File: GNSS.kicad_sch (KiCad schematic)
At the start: 16 parts, among them J10 USB_C_USB2.0_16P, J11 Micro_SD_Card, J12 RF SMA, SW3 SW_Push, U6 NEO-M9N

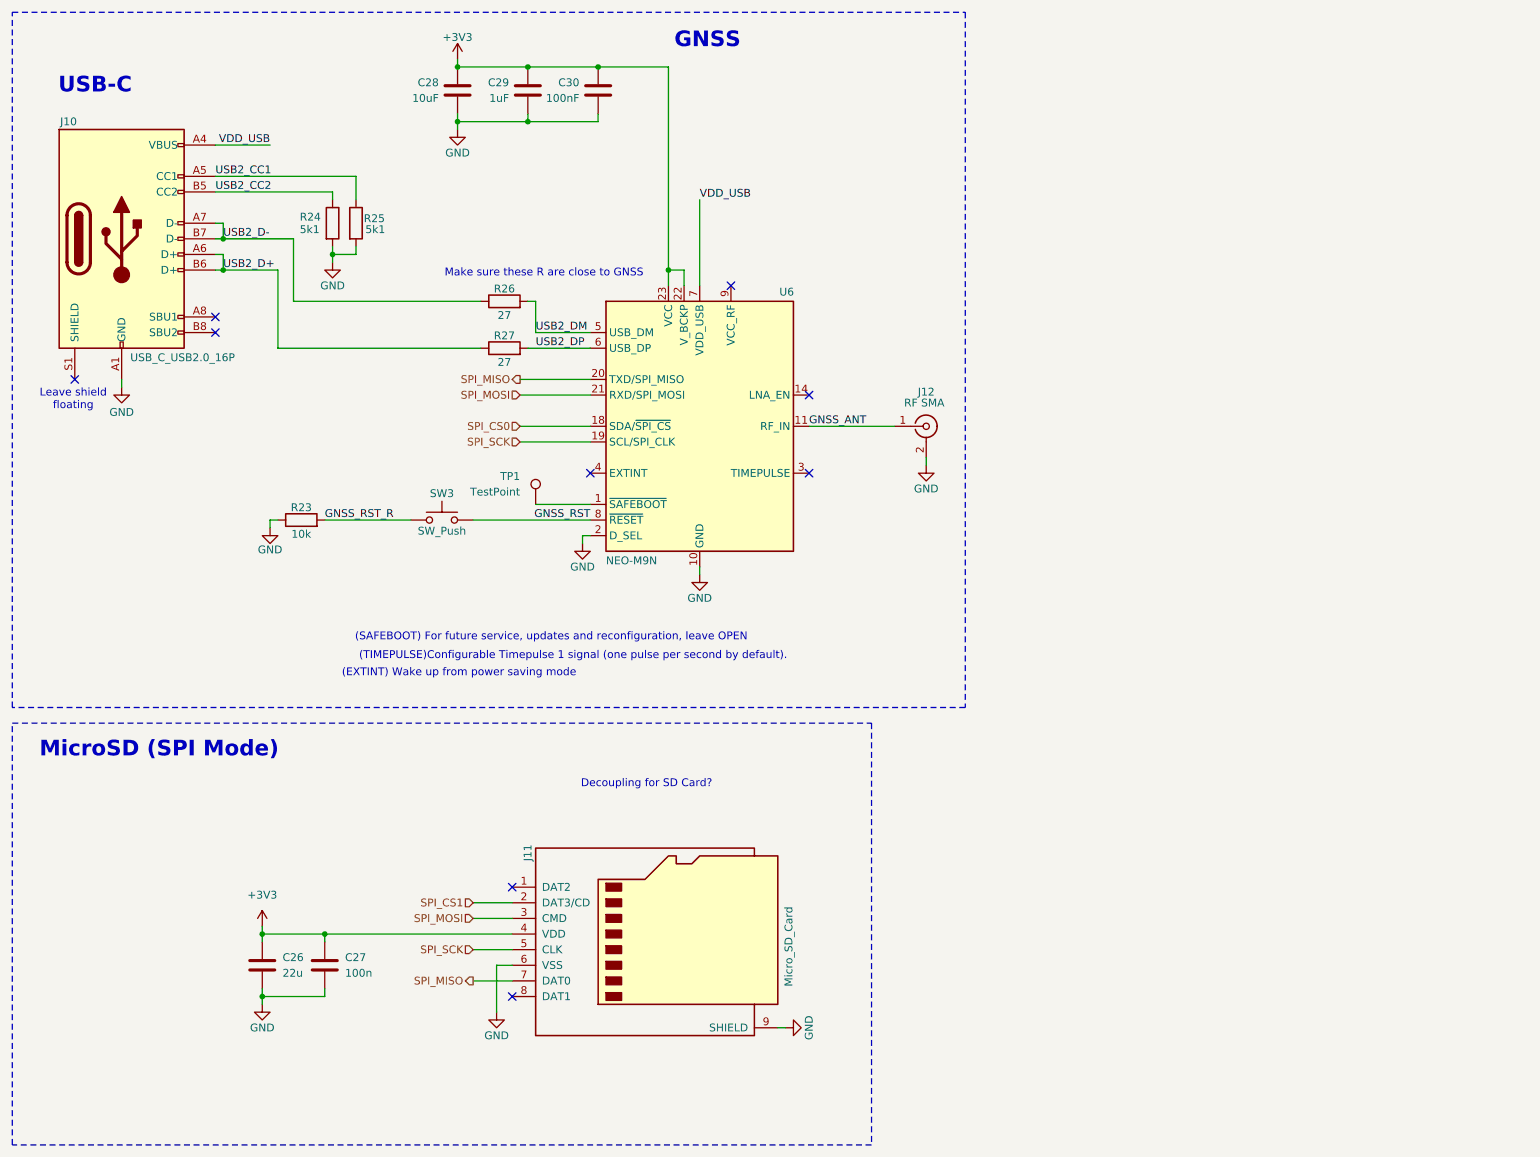
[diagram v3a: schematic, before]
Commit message: Added 3D models and LCSC part numbers
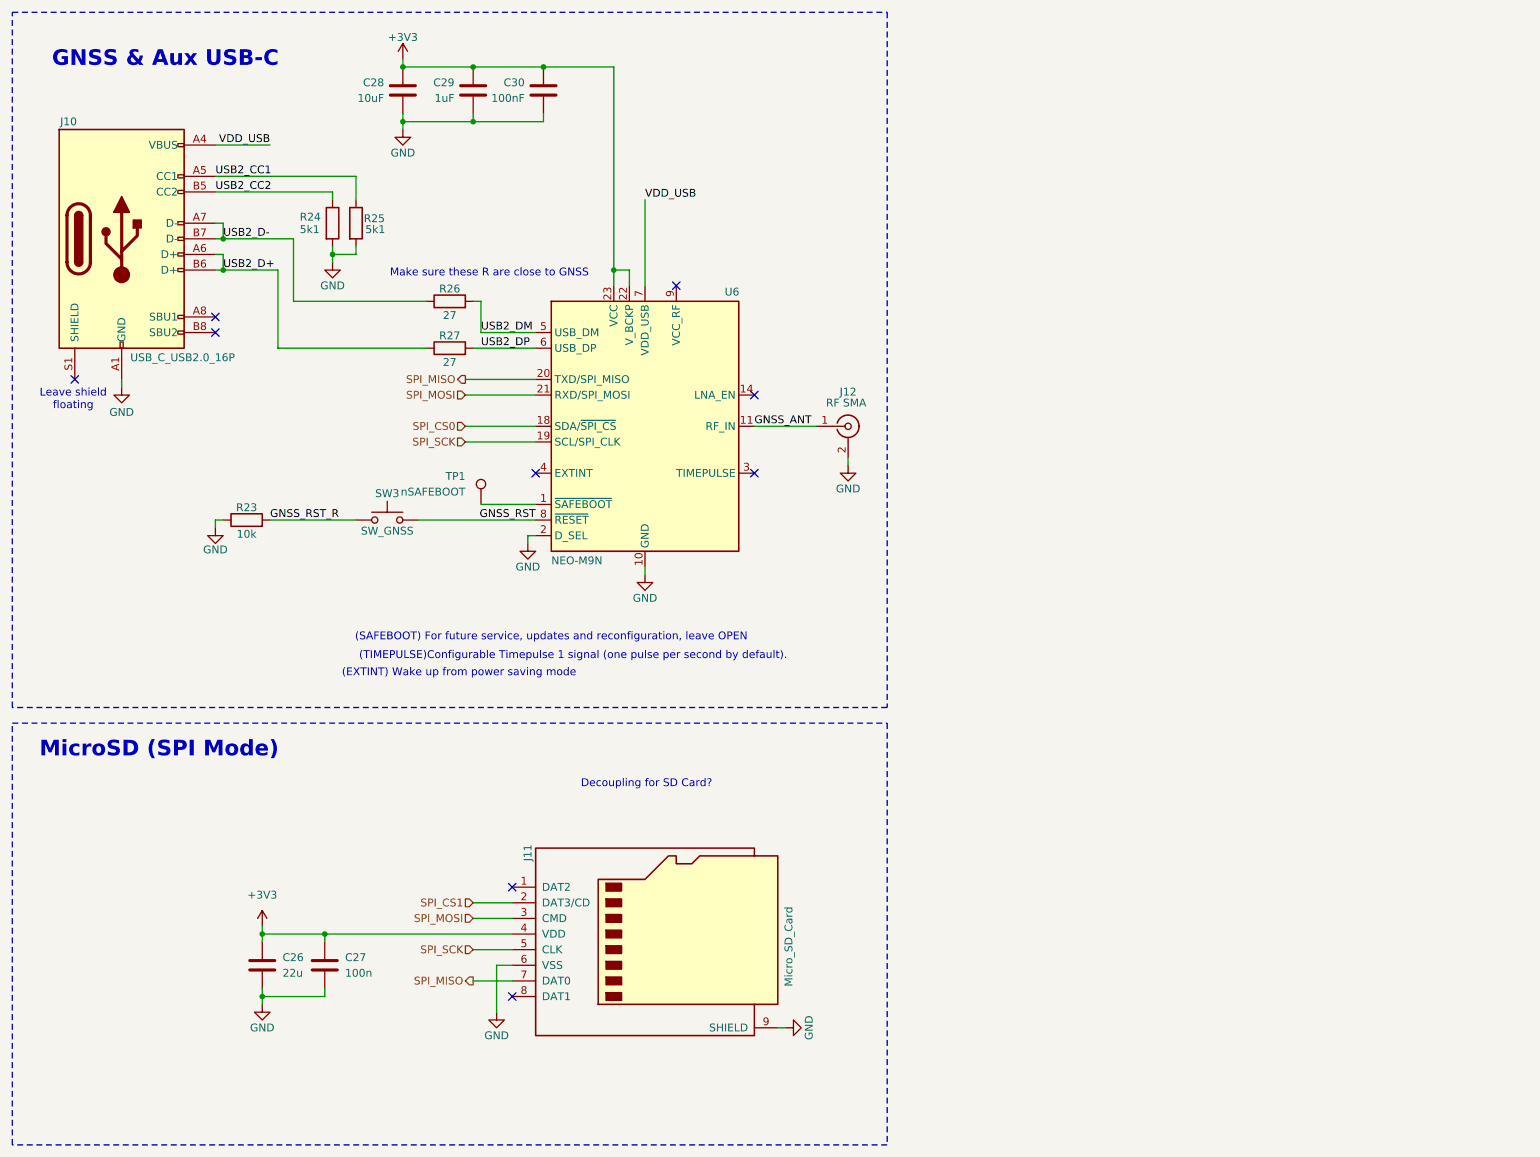
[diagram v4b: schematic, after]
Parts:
- J10: LCSC Part (none) -> C165948
- SW3: value SW_Push -> SW_GNSS
- TP1: value TestPoint -> nSAFEBOOT
- U6: LCSC Part (none) -> C5119087
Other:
- note added: "GNSS & Aux USB-C"
- note removed: "GNSS"
- note removed: "USB-C"
- moved on the sheet: C28, C29, C30, J12, R23, R26, R27, SW3, TP1, U6

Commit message: General DFM fixes
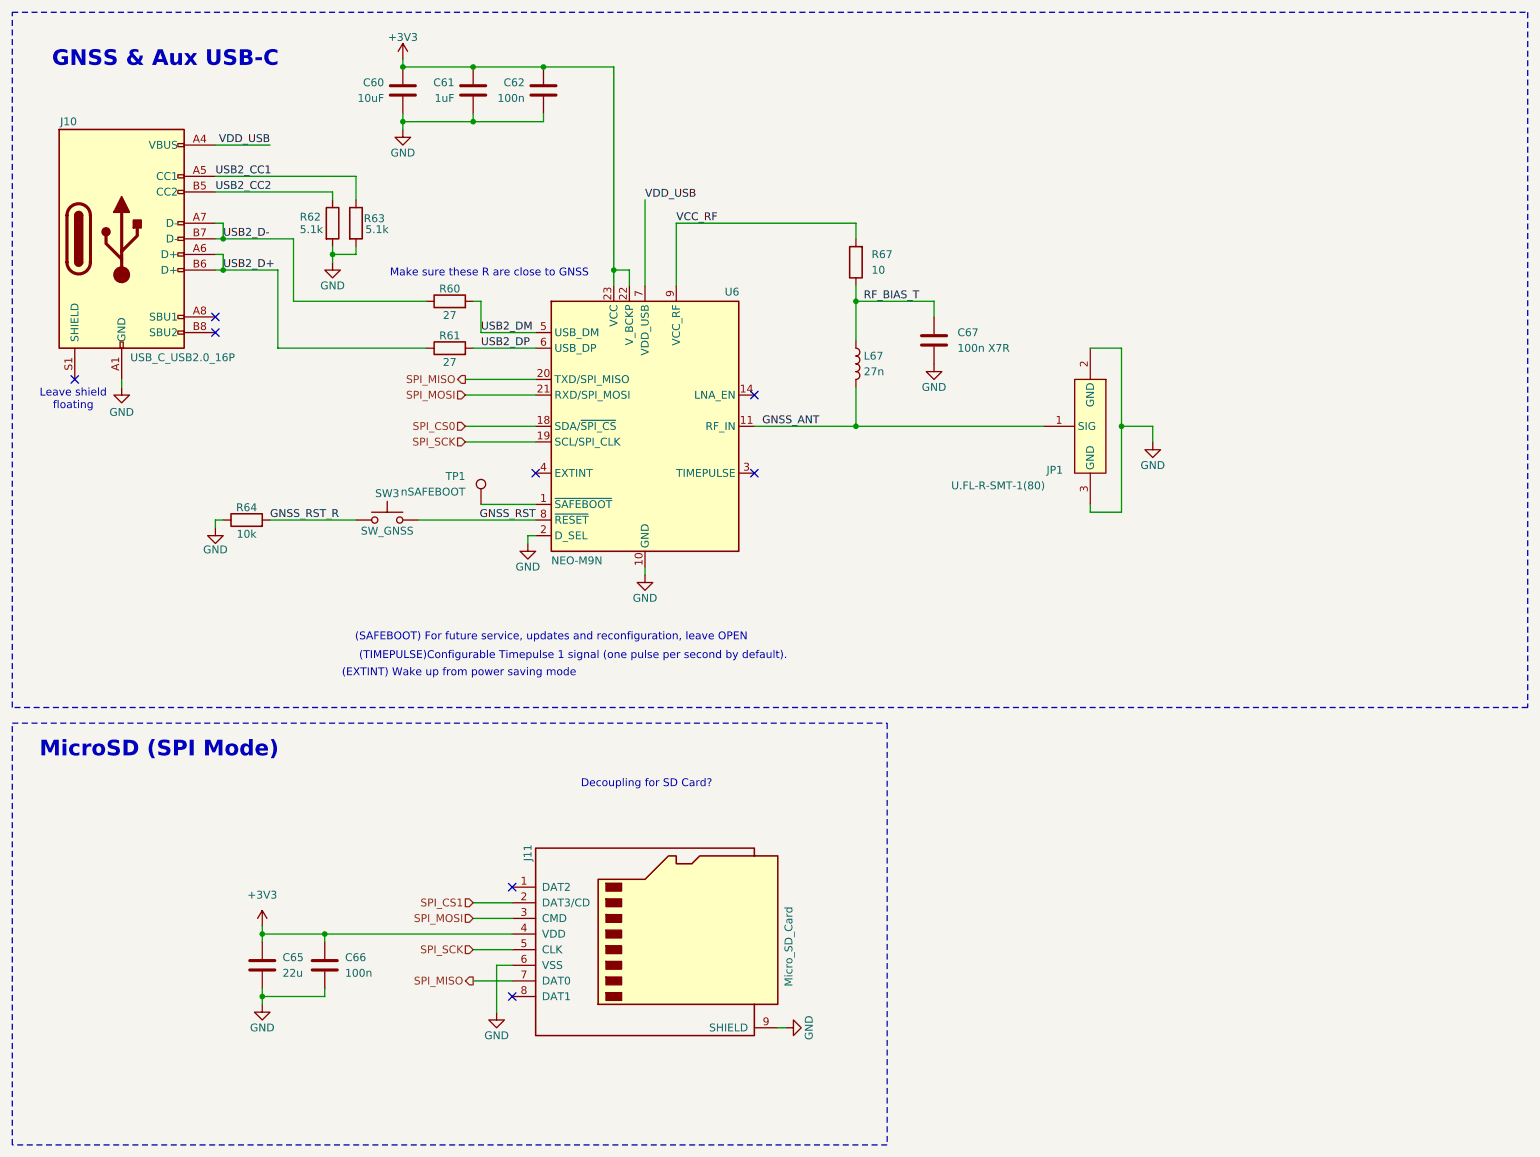
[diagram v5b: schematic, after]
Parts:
- removed J12: RF SMA, Connector_Coaxial:SMA_Amphenol_132134_Vertical, symbol Connector:Conn_Coaxial
- added C67: 100n X7R, Capacitor_SMD:C_0402_1005Metric, symbol Device:C
- added JP1: U.FL-R-SMT-1(80), easyeda2kicad:RF-SMD_FRF05002-JSS103M, symbol easyeda2kicad:U.FL-R-SMT-1(80)
- added L67: 27n, Inductor_SMD:L_0201_0603Metric, symbol Device:L
- added R67: 10, Resistor_SMD:R_0805_2012Metric, symbol Device:R
- C62: renamed from C30; value 100nF -> 100n
- C66: renamed from C27; LCSC Part (none) -> C1525
- J11: footprint Connector_Card:microSD_HC_Wuerth_693072010801 -> Connector_Card:microSD_HC_Molex_47219-2001; LCSC Part (none) -> C164170
- R62: renamed from R24; value 5k1 -> 5.1k
- R63: renamed from R25; value 5k1 -> 5.1k
- SW3: LCSC Part (none) -> C720477
- renumbered C28 to C60, C29 to C61, C26 to C65, R26 to R60, R27 to R61, R23 to R64
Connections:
- net GND: now also C67.2, JP1.2 (GND), JP1.3 (GND)
- net GNSS_ANT: now also JP1.1 (SIG), L67.2
- net VCC_RF: now reaches U6.9 (VCC_RF)
- net VCC_RF: now also R67.2
- new net RF_BIAS_T: C67.1, L67.1, R67.1
- no-connect marks 9 -> 8
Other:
- title: GNSS NEO-M6N -> GNSS NEO-M9N
